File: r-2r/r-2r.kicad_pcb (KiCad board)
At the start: 2 copper layers, 26 parts, among them J1 D7, J10 Gnd, J2 D6, J3 D5, J4 D4, J5 D3, J6 D2, J7 D1, J8 D0, J9 Out

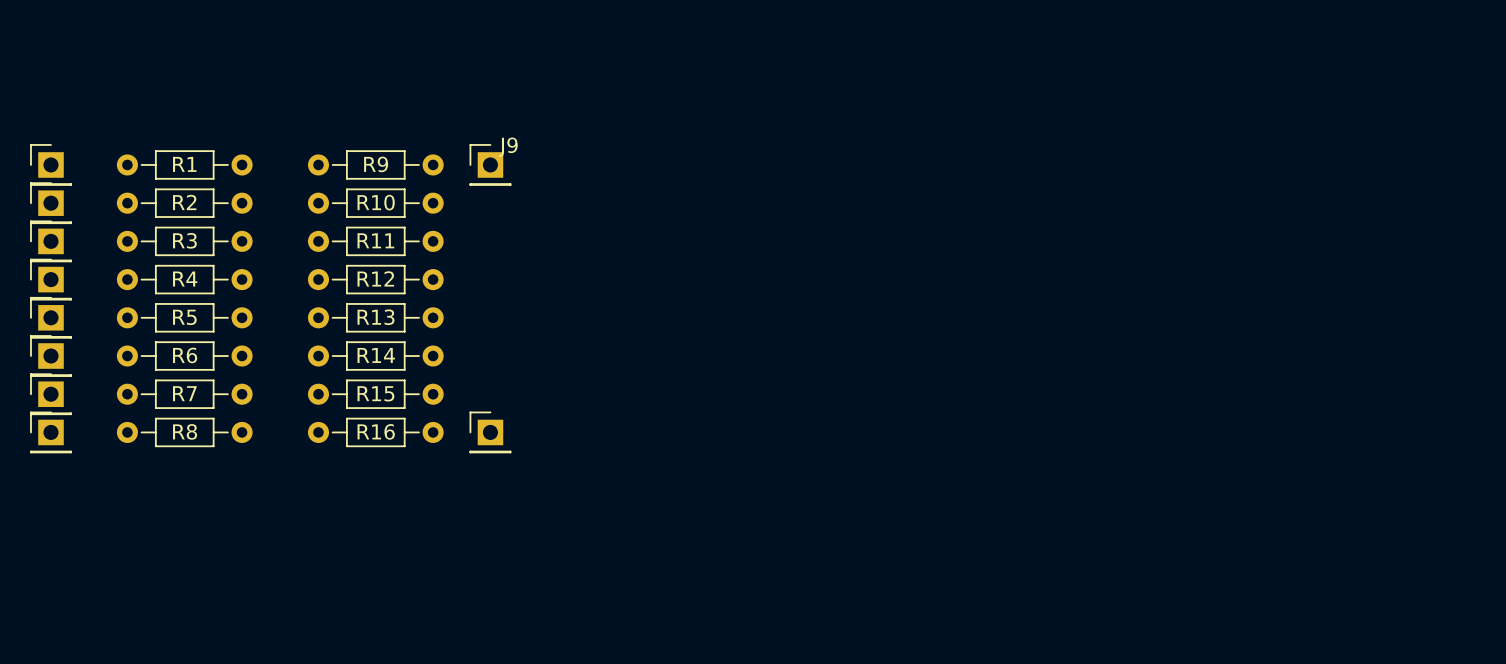
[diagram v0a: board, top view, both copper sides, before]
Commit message: Add mounting holes
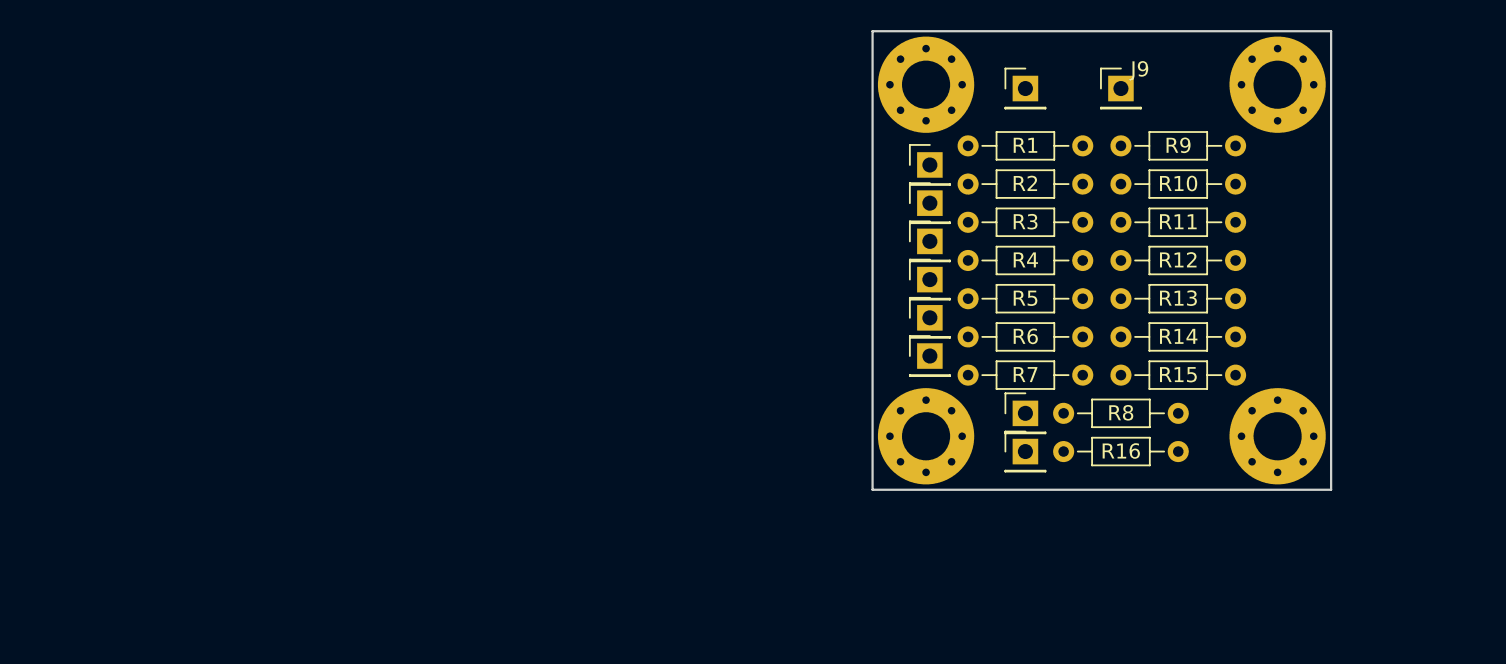
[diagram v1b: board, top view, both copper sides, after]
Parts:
- added MH1: MountingHole, MountingHole:MountingHole_3.2mm_M3_Pad_Via, F.Cu at (135.6, 37.8)
- added MH2: MountingHole, MountingHole:MountingHole_3.2mm_M3_Pad_Via, F.Cu at (135.6, 61.2)
- added MH3: MountingHole, MountingHole:MountingHole_3.2mm_M3_Pad_Via, F.Cu at (159.0, 37.8)
- added MH4: MountingHole, MountingHole:MountingHole_3.2mm_M3_Pad_Via, F.Cu at (159.0, 61.2)
- moved J1 65.0 mm to (142.2, 38.1)
- moved J8 64.8 mm to (142.2, 59.7)
- moved R8 62.2 mm to (152.4, 59.7)
- moved J2 58.5 mm to (135.9, 43.2)
- moved J3 58.5 mm to (135.9, 45.7)
- moved J4 58.5 mm to (135.9, 48.3)
- moved J5 58.5 mm to (135.9, 50.8)
- moved J6 58.5 mm to (135.9, 53.3)
- moved J7 58.5 mm to (135.9, 55.9)
- moved R16 57.2 mm to (152.4, 62.2), turned to 180 degrees
- moved R1 55.9 mm to (146.1, 41.9)
- moved R2 55.9 mm to (146.1, 44.5)
- moved R3 55.9 mm to (146.1, 47.0)
- moved R4 55.9 mm to (146.1, 49.5)
- moved R5 55.9 mm to (146.1, 52.1)
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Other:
- board outline added: 30.5 x 30.5 mm

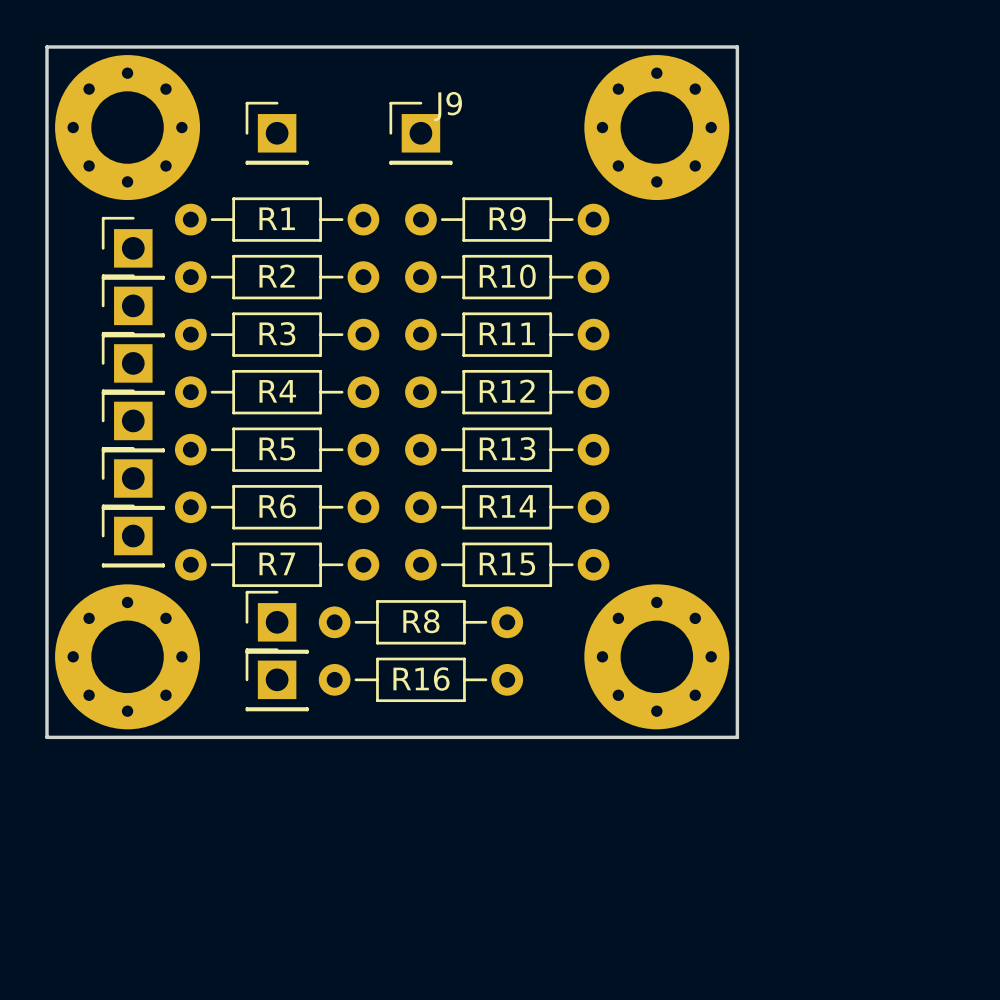
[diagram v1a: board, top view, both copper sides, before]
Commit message: Enlarge pcb to 40 x 40
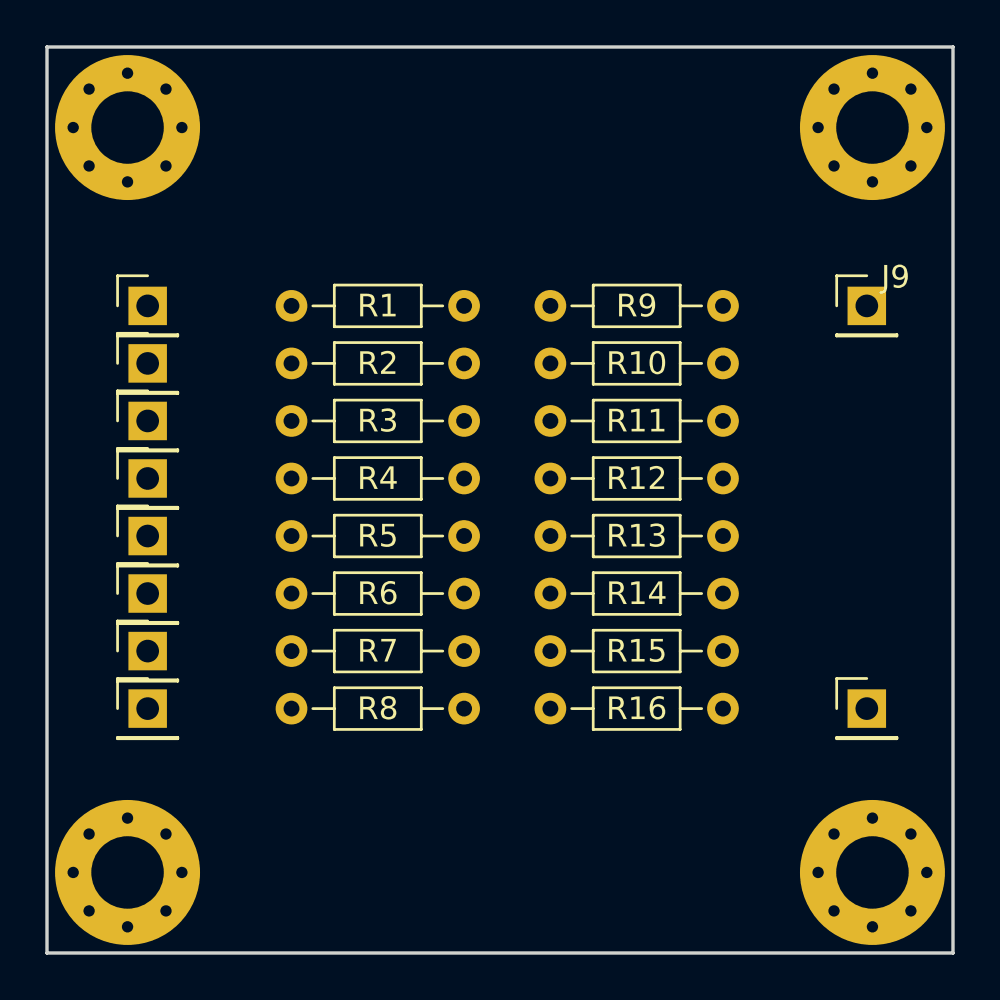
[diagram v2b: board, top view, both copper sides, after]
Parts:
- moved J10 26.1 mm to (168.3, 63.5)
- moved J9 21.1 mm to (168.3, 45.7)
- moved MH4 13.5 mm to (168.5, 70.7)
- moved J1 9.53 mm to (136.5, 45.7)
- moved MH3 9.52 mm to (168.5, 37.8)
- moved MH2 9.52 mm to (135.6, 70.7)
- moved J8 6.87 mm to (136.5, 63.5)
- moved R12 6.87 mm to (154.3, 53.3)
- moved R13 6.87 mm to (154.3, 55.9)
- moved R14 6.87 mm to (154.3, 58.4)
- moved R15 6.87 mm to (154.3, 61.0)
- moved R9 6.87 mm to (154.3, 45.7)
- moved R10 6.87 mm to (154.3, 48.3)
- moved R11 6.87 mm to (154.3, 50.8)
- moved R1 5.85 mm to (150.5, 45.7)
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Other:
- board size 30.5 x 30.5 mm -> 40 x 40 mm

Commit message: R-2R ready
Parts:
- moved J1 0.64 mm to (135.9, 45.7)
- moved J2 0.64 mm to (135.9, 48.3)
- moved J3 0.64 mm to (135.9, 50.8)
- moved J4 0.64 mm to (135.9, 53.3)
- moved J5 0.64 mm to (135.9, 55.9)
- moved J6 0.64 mm to (135.9, 58.4)
- moved J7 0.64 mm to (135.9, 61.0)
- moved J8 0.64 mm to (135.9, 63.5)
- moved R10 0.64 mm to (153.7, 48.3)
- moved R11 0.64 mm to (153.7, 50.8)
- moved R12 0.64 mm to (153.7, 53.3)
- moved R13 0.64 mm to (153.7, 55.9)
- moved R14 0.64 mm to (153.7, 58.4)
- moved R15 0.64 mm to (153.7, 61.0)
- moved R16 0.64 mm to (153.7, 63.5)
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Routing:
- net Net-(J9-Pad1): track 0.00 -> 20.5 mm
- net Net-(R11-Pad2): track 0.00 -> 12.5 mm
- net Net-(R15-Pad2): track 0.00 -> 12.5 mm
- net Net-(R14-Pad2): track 0.00 -> 12.5 mm
- net Net-(R13-Pad2): track 0.00 -> 12.5 mm
- net Net-(R12-Pad2): track 0.00 -> 12.5 mm
- net Net-(R10-Pad2): track 0.00 -> 12.5 mm
- net Net-(R10-Pad1): track 0.00 -> 12.5 mm
- net GND: track 0.00 -> 6.99 mm
- net Net-(J8-Pad1): track 0.00 -> 6.35 mm
- net Net-(J7-Pad1): track 0.00 -> 6.35 mm
- net Net-(J6-Pad1): track 0.00 -> 6.35 mm
- net Net-(J5-Pad1): track 0.00 -> 6.35 mm
- net Net-(J4-Pad1): track 0.00 -> 6.35 mm
- net Net-(J3-Pad1): track 0.00 -> 6.35 mm
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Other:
- board text added: "D0"
- board text added: "D1"
- board text added: "D2"
- board text added: "D3"
- board text added: "D4"
- board text added: "D5"
- board text added: "D6"
- board text added: "D7"
- board text added: "Gnd"
- board text added: "Out"
